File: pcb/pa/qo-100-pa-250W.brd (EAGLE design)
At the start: 156 x 60 mm, 1 part

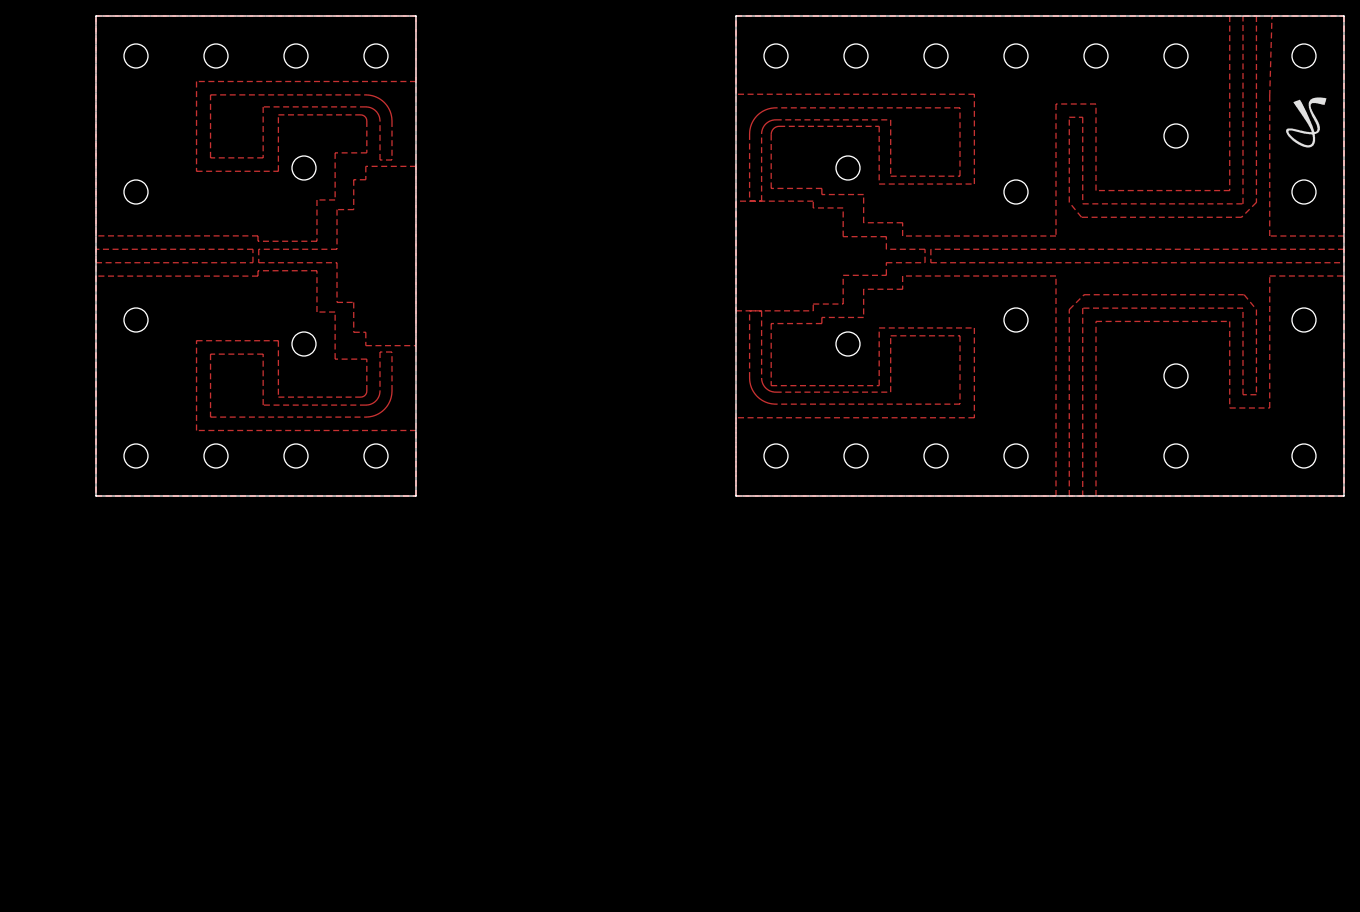
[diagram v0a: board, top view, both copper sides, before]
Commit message: Changes to PA PCBs for easier etching
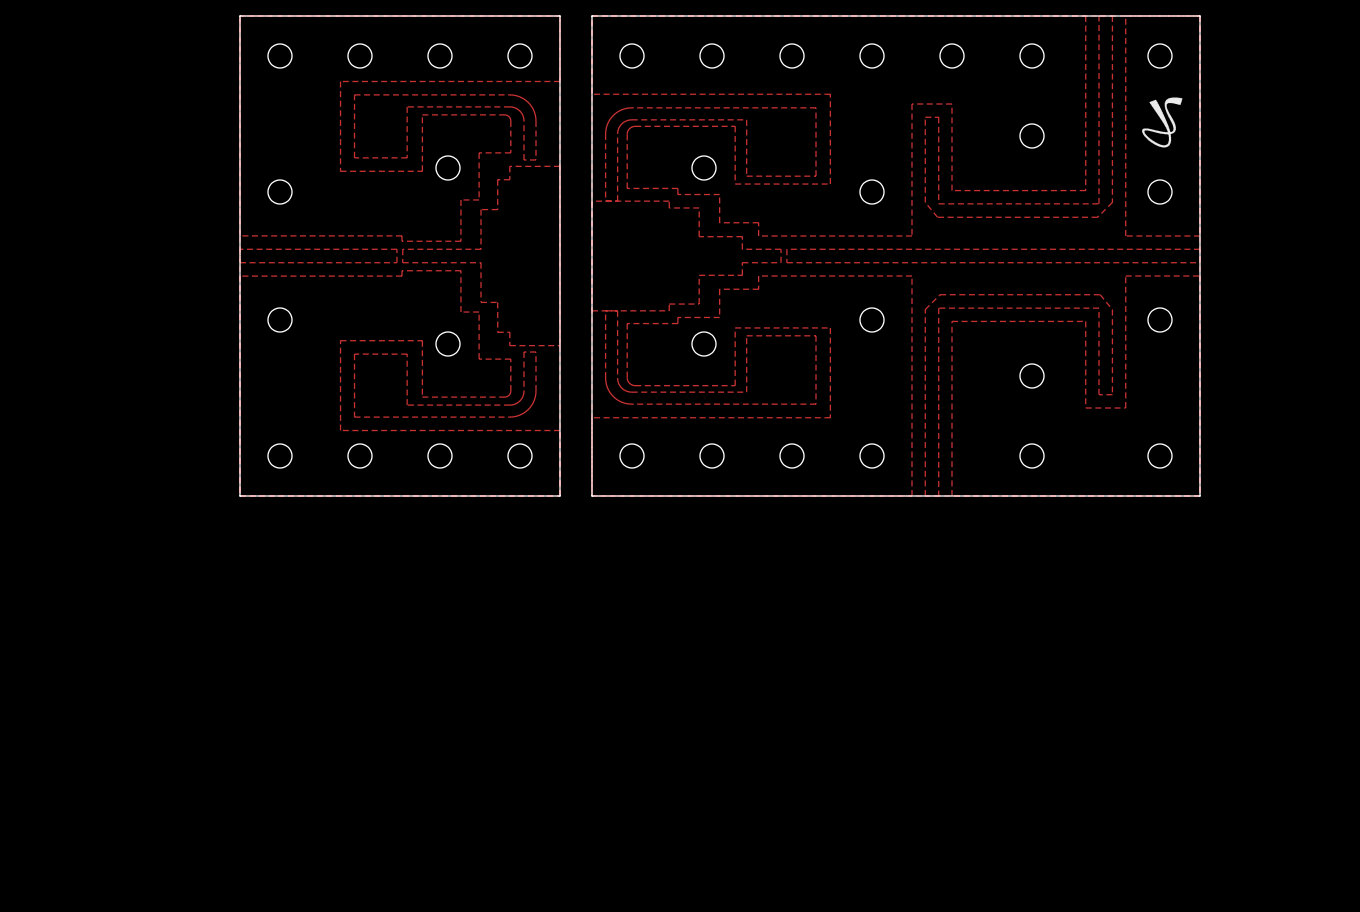
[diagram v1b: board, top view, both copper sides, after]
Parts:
- moved E$1 18.0 mm to (76.0, 50.0)
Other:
- board size 156 x 60 mm -> 120 x 60 mm

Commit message: Update PA PCBs
Signed-off-by: João Silva <jgc3silva@gmail.com>
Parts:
- moved E$1 3.00 mm to (79.0, 50.0)
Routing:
- added copper zone on layer 1, net IN2
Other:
- board size 120 x 60 mm -> 150 x 60 mm

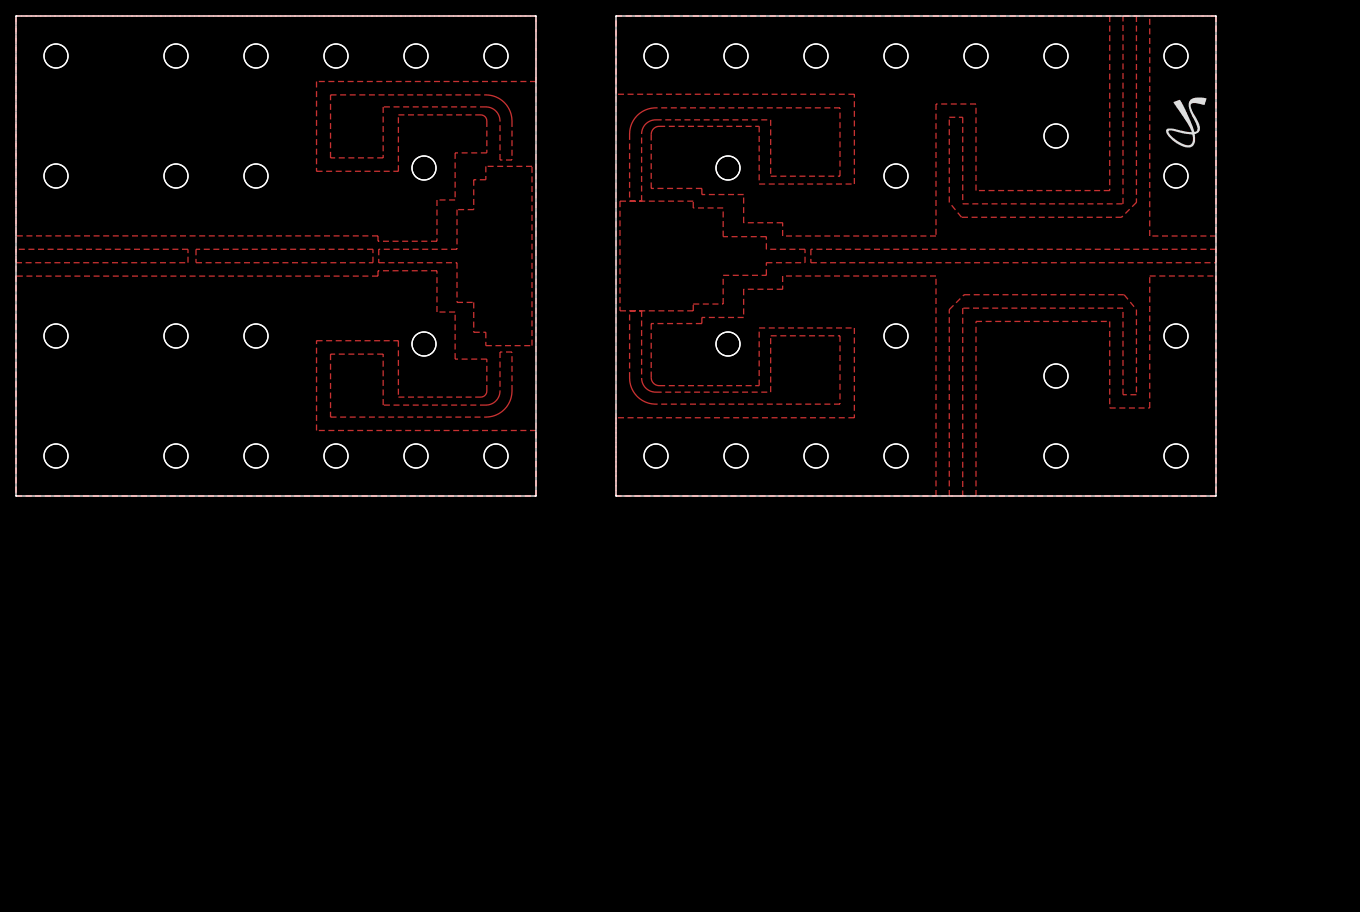
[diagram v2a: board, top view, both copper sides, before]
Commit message: Modify 250W PA PCB to fit heat spreader
Signed-off-by: João Silva <jgc3silva@gmail.com>
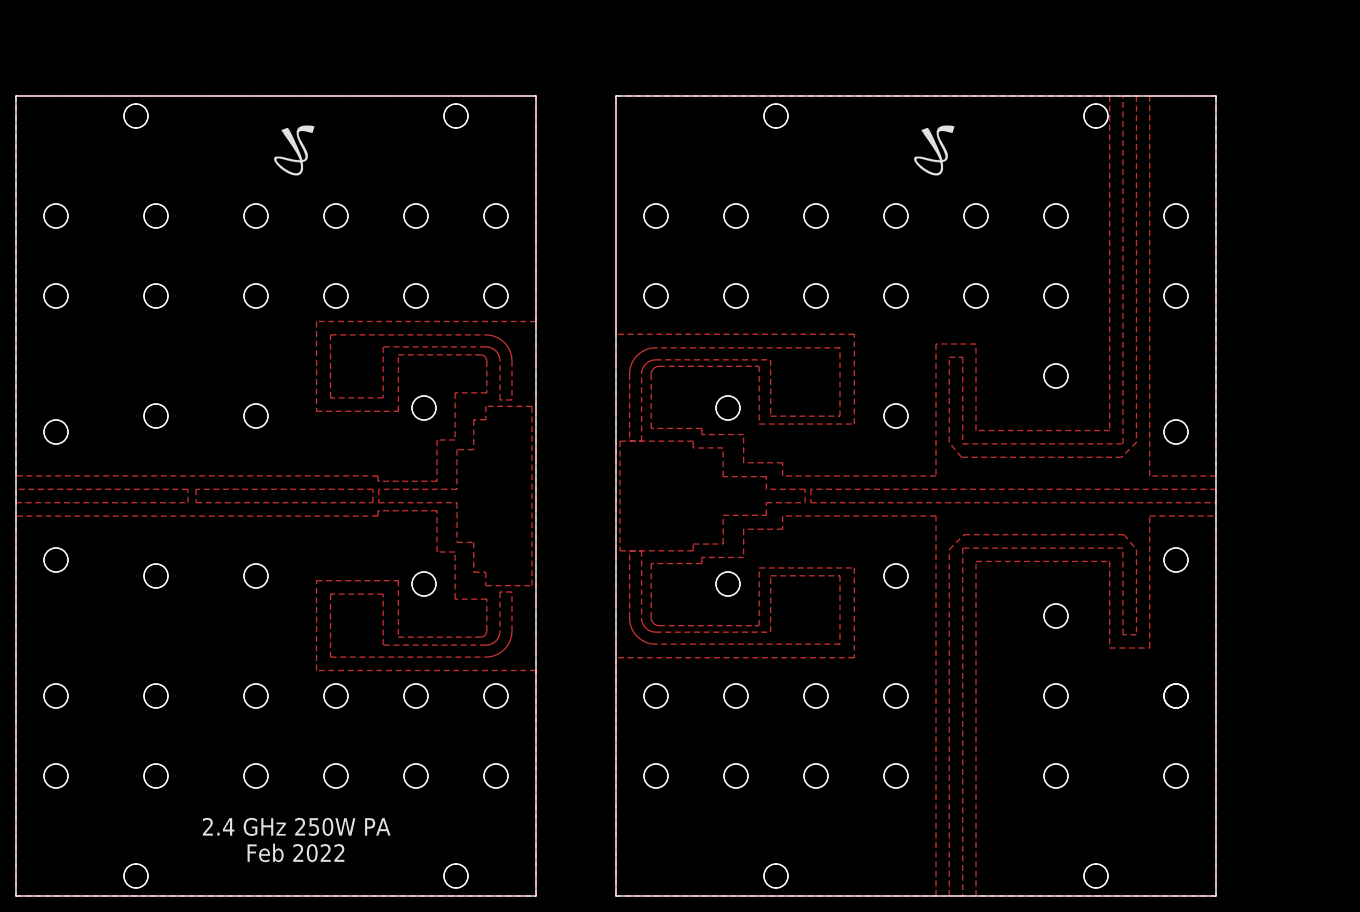
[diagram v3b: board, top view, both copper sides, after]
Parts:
- added E$2: (no value), Silkscreen:JS_5MM
- moved E$1 31.7 mm to (47.5, 46.5)
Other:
- board size 150 x 60 mm -> 150 x 100 mm
- board text added: "2.4 GHz 250W PA Feb 2022"
